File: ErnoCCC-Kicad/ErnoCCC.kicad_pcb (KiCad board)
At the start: 2 copper layers, 161.4 x 95.9 mm, 96 parts, among them J1 6VAC, J2 ICSP, J3 FTDI, J4 Erno Controller, J5 SWITCH, J6 LED OUT, J7 Conn_01x05, Q1 BC847, Q2 BC847, SW1 SW_Push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

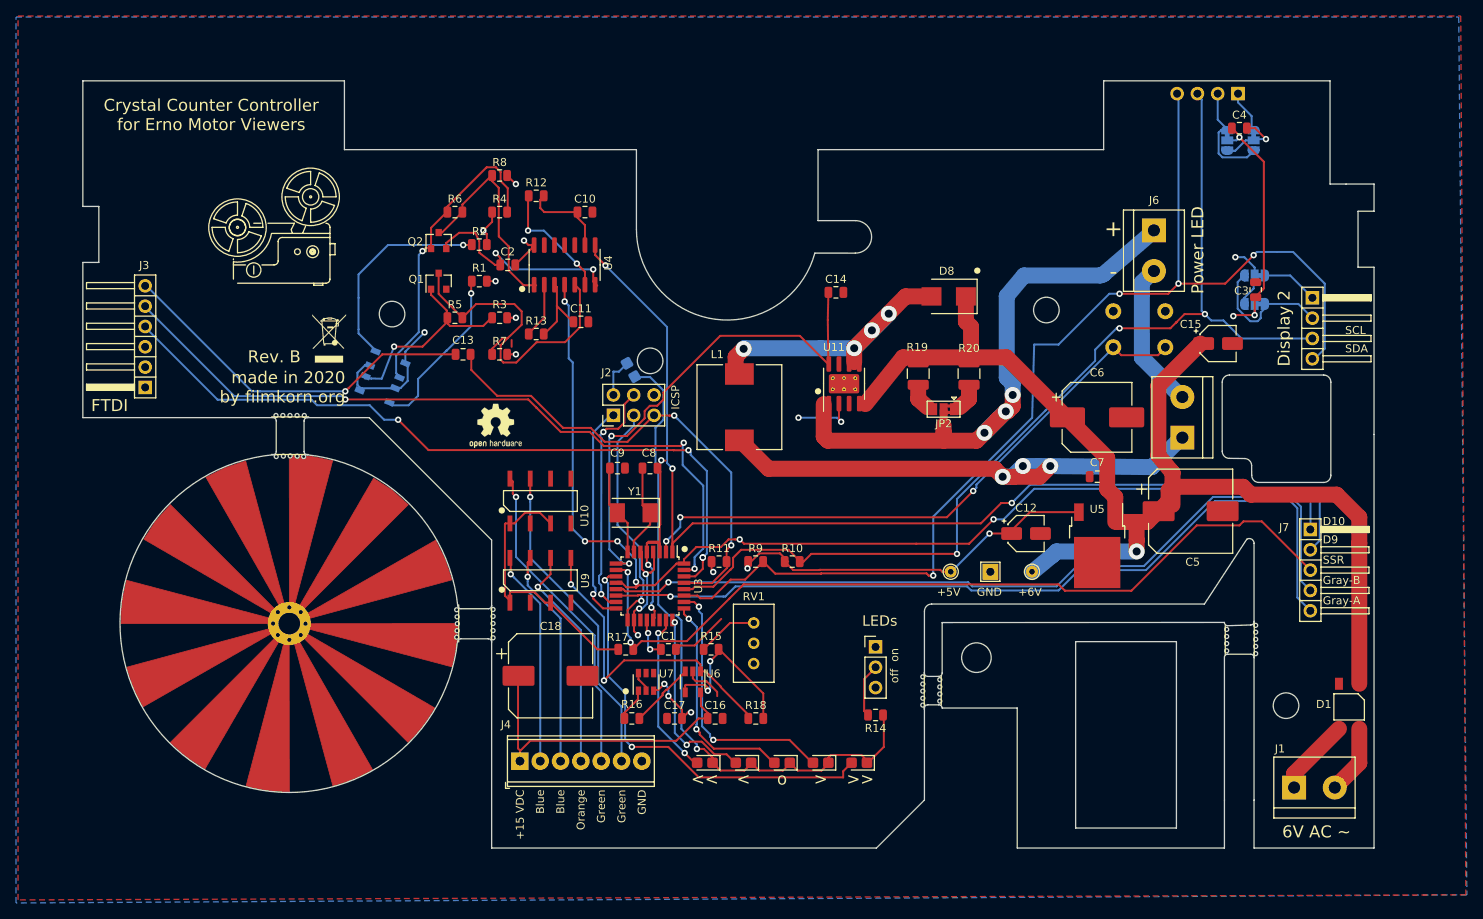
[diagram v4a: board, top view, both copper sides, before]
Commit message: Rounding Corners, making fidicules actually match
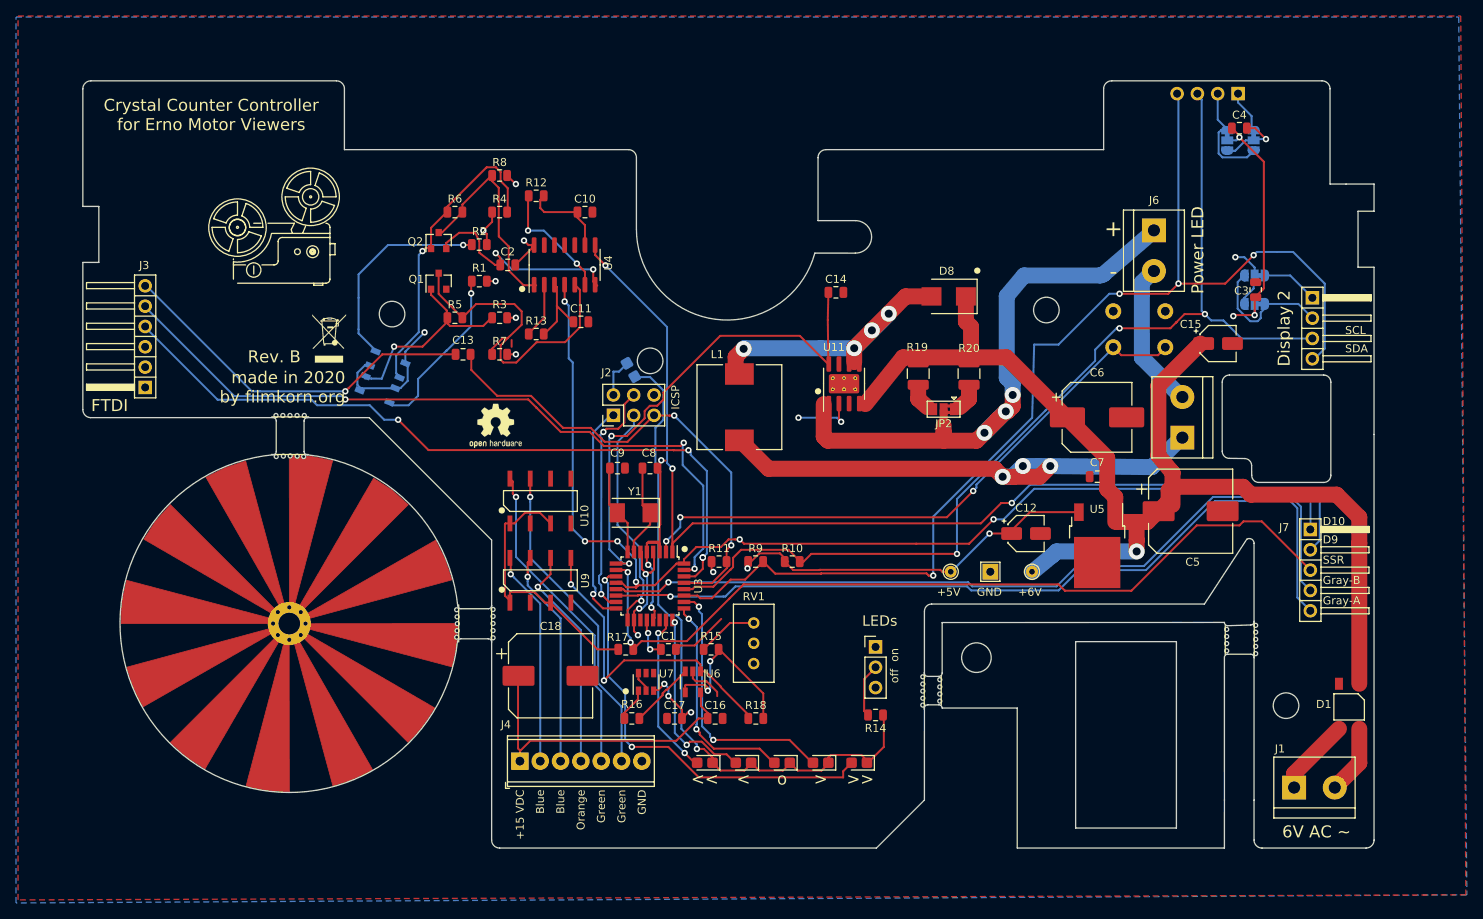
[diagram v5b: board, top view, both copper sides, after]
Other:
- outline, holes or cut-outs redrawn
- board text added: "Cut/Shorten both Jumpers to swap Display polarity"
- board text removed: "Cut/Shorten both Jumpers to swap Display ploarity"
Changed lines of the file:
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@@
   (general
     (thickness 1.6)
-    (drawings 313)
+    (drawings 324)
     (tracks 992)
     (zones 0)
@@
     )
   )
+  (gr_arc (start 218.1 26.2) (end 219.1 26.2) (angle -90) (layer Edge.Cuts) (width 0.05))
+  (gr_arc (start 191.8 26.2) (end 191.8 25.2) (angle -90) (layer Edge.Cuts) (width 0.05))
+  (gr_arc (start 94.9 26.2) (end 95.9 26.2) (angle -90) (layer Edge.Cuts) (width 0.05))
+  (gr_arc (start 64.2 26.2) (end 64.2 25.2) (angle -90) (layer Edge.Cuts) (width 0.05))
+  (gr_arc (start 64.2 66.3) (end 63.2 66.3) (angle -90) (layer Edge.Cuts) (width 0.05))
+  (gr_arc (start 115.3 120.1) (end 114.3 120.1) (angle -90) (layer Edge.Cuts) (width 0.05))
+  (gr_arc (start 223.6 120.1) (end 223.6 121.1) (angle -90) (layer Edge.Cuts) (width 0.05))
+  (gr_arc (start 210.6 120.1) (end 209.6 120.1) (angle -90) (layer Edge.Cuts) (width 0.05))
+  (gr_arc (start 156.1 34.8) (end 156.1 33.8) (angle -90) (layer Edge.Cuts) (width 0.05))
+  (gr_arc (start 131.4 34.8) (end 132.4 34.8) (angle -90) (layer Edge.Cuts) (width 0.05))
+  (gr_circle (center 231.7 71.1) (end 234.7 71.1) (layer F.Paste) (width 0.01))
   (gr_circle (center 52.2 121.1) (end 55.2 121.1) (layer F.Paste) (width 0.01))
   (gr_circle (center 52.2 25.2) (end 55.2 25.2) (layer F.Paste) (width 0.01))
@@
     (effects (font (size 1 1) (thickness 0.15)) (justify right))
   )
-  (gr_text "Cut/Shorten \nboth Jumpers \nto swap Display \nploarity" (at 204 33.1) (layer B.SilkS)
+  (gr_text "Cut/Shorten \nboth Jumpers \nto swap Display \npolarity" (at 204 33.1) (layer B.SilkS)
     (effects (font (size 1 1) (thickness 0.15)) (justify left mirror))
   )
@@
   (gr_line (start 168.401874 103.6066) (end 168.4 115.1) (layer Edge.Cuts) (width 0.05))
   (gr_line (start 205.901874 115.114) (end 205.9 121.1) (layer Edge.Cuts) (width 0.05))
-  (gr_line (start 209.6 115.1) (end 209.6 121.1) (layer Edge.Cuts) (width 0.05))
+  (gr_line (start 209.6 115.1) (end 209.6 120.1) (layer Edge.Cuts) (width 0.05))
   (gr_line (start 170.6118 92.9132) (end 170.6118 99.2378) (layer Edge.Cuts) (width 0.05))
   (gr_line (start 180 103.6) (end 170.6118 103.6) (layer Edge.Cuts) (width 0.05))
@@
   (gr_line (start 209.6 97.282) (end 209.6 115.1) (layer Edge.Cuts) (width 0.05))
   (gr_line (start 209.6008 92.8116) (end 209.6 83) (layer Edge.Cuts) (width 0.05))
-  (gr_line (start 224.6 69.4) (end 224.6 121.1) (layer Edge.Cuts) (width 0.05))
-  (gr_line (start 209.6 121.1) (end 224.6 121.1) (layer Edge.Cuts) (width 0.05))
+  (gr_line (start 224.6 69.4) (end 224.6 120.1) (layer Edge.Cuts) (width 0.05))
+  (gr_line (start 210.6 121.1) (end 223.6 121.1) (layer Edge.Cuts) (width 0.05))
   (gr_arc (start 218.313 62.865) (end 219.202 62.865) (angle -90) (layer Edge.Cuts) (width 0.05))
   (gr_arc (start 206.513 62.865) (end 206.513 61.976) (angle -90) (layer Edge.Cuts) (width 0.05))
@@
   (gr_arc (start 143.75 43.75) (end 132.4 43.75) (angle -164.7617781) (layer Edge.Cuts) (width 0.05))
   (gr_line (start 168.4 115.1) (end 162.4 121.1) (layer Edge.Cuts) (width 0.05))
-  (gr_line (start 63.2 40.9) (end 63.2 25.2) (layer Edge.Cuts) (width 0.05))
+  (gr_line (start 63.2 40.9) (end 63.2 26.2) (layer Edge.Cuts) (width 0.05))
   (gr_line (start 65.2 40.9) (end 63.2 40.9) (layer Edge.Cuts) (width 0.05))
   (gr_line (start 65.2 47.9) (end 65.2 40.9) (layer Edge.Cuts) (width 0.05))
   (gr_line (start 63.2 47.9) (end 65.2 47.9) (layer Edge.Cuts) (width 0.05))
-  (gr_line (start 63.2 67.3) (end 63.2 47.9) (layer Edge.Cuts) (width 0.05))
-  (gr_line (start 86.9696 67.3) (end 63.2 67.3) (layer Edge.Cuts) (width 0.05))
+  (gr_line (start 63.2 66.3) (end 63.2 47.9) (layer Edge.Cuts) (width 0.05))
+  (gr_line (start 86.9696 67.3) (end 64.2 67.3) (layer Edge.Cuts) (width 0.05))
   (gr_line (start 114.3 82.6) (end 99 67.3) (layer Edge.Cuts) (width 0.05))
-  (gr_line (start 114.3 121.1) (end 114.3 95.3516) (layer Edge.Cuts) (width 0.05))
-  (gr_line (start 162.4 121.1) (end 114.3 121.1) (layer Edge.Cuts) (width 0.05))
+  (gr_line (start 114.3 120.1) (end 114.3 95.3516) (layer Edge.Cuts) (width 0.05))
+  (gr_line (start 162.4 121.1) (end 115.3 121.1) (layer Edge.Cuts) (width 0.05))
   (gr_line (start 168.4 91.5) (end 168.4 99.2378) (layer Edge.Cuts) (width 0.05))
   (gr_line (start 203.4 90.6) (end 169.3 90.6) (layer Edge.Cuts) (width 0.05))
@@
   (gr_line (start 221.1 38.1) (end 224.6 38.1) (layer Edge.Cuts) (width 0.05))
   (gr_line (start 219.1 38.1) (end 221.1 38.1) (layer Edge.Cuts) (width 0.05))
-  (gr_line (start 219.1 25.2) (end 219.1 38.1) (layer Edge.Cuts) (width 0.05))
-  (gr_line (start 190.8 25.2) (end 219.1 25.2) (layer Edge.Cuts) (width 0.05))
-  (gr_line (start 190.8 33.8) (end 190.8 25.2) (layer Edge.Cuts) (width 0.05))
-  (gr_line (start 155.1 33.8) (end 190.8 33.8) (layer Edge.Cuts) (width 0.05))
-  (gr_line (start 155.1 42.672) (end 155.1 33.8) (layer Edge.Cuts) (width 0.05))
-  (gr_line (start 132.4 33.8) (end 132.4 43.75) (layer Edge.Cuts) (width 0.05))
-  (gr_line (start 95.9 33.8) (end 132.4 33.8) (layer Edge.Cuts) (width 0.05))
-  (gr_line (start 95.9 25.2) (end 95.9 33.8) (layer Edge.Cuts) (width 0.05))
-  (gr_line (start 63.2 25.2) (end 95.9 25.2) (layer Edge.Cuts) (width 0.05))
+  (gr_line (start 219.1 26.2) (end 219.1 38.1) (layer Edge.Cuts) (width 0.05))
+  (gr_line (start 191.8 25.2) (end 218.1 25.2) (layer Edge.Cuts) (width 0.05))
+  (gr_line (start 190.8 33.8) (end 190.8 26.2) (layer Edge.Cuts) (width 0.05))
+  (gr_line (start 156.1 33.8) (end 190.8 33.8) (layer Edge.Cuts) (width 0.05))
+  (gr_line (start 155.1 42.672) (end 155.1 34.8) (layer Edge.Cuts) (width 0.05))
+  (gr_line (start 132.4 34.8) (end 132.4 43.75) (layer Edge.Cuts) (width 0.05))
+  (gr_line (start 95.9 33.8) (end 131.4 33.8) (layer Edge.Cuts) (width 0.05))
+  (gr_line (start 95.9 26.2) (end 95.9 33.8) (layer Edge.Cuts) (width 0.05))
+  (gr_line (start 64.2 25.2) (end 94.9 25.2) (layer Edge.Cuts) (width 0.05))
   (gr_arc (start 90.025 43.765) (end 89.263 43.765) (angle -30.96375653) (layer F.SilkS) (width 0.12))
   (gr_line (start 91.041 43.384) (end 90.66 44.273) (layer F.SilkS) (width 0.12))

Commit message: Preparing RevC. One Diode still missing
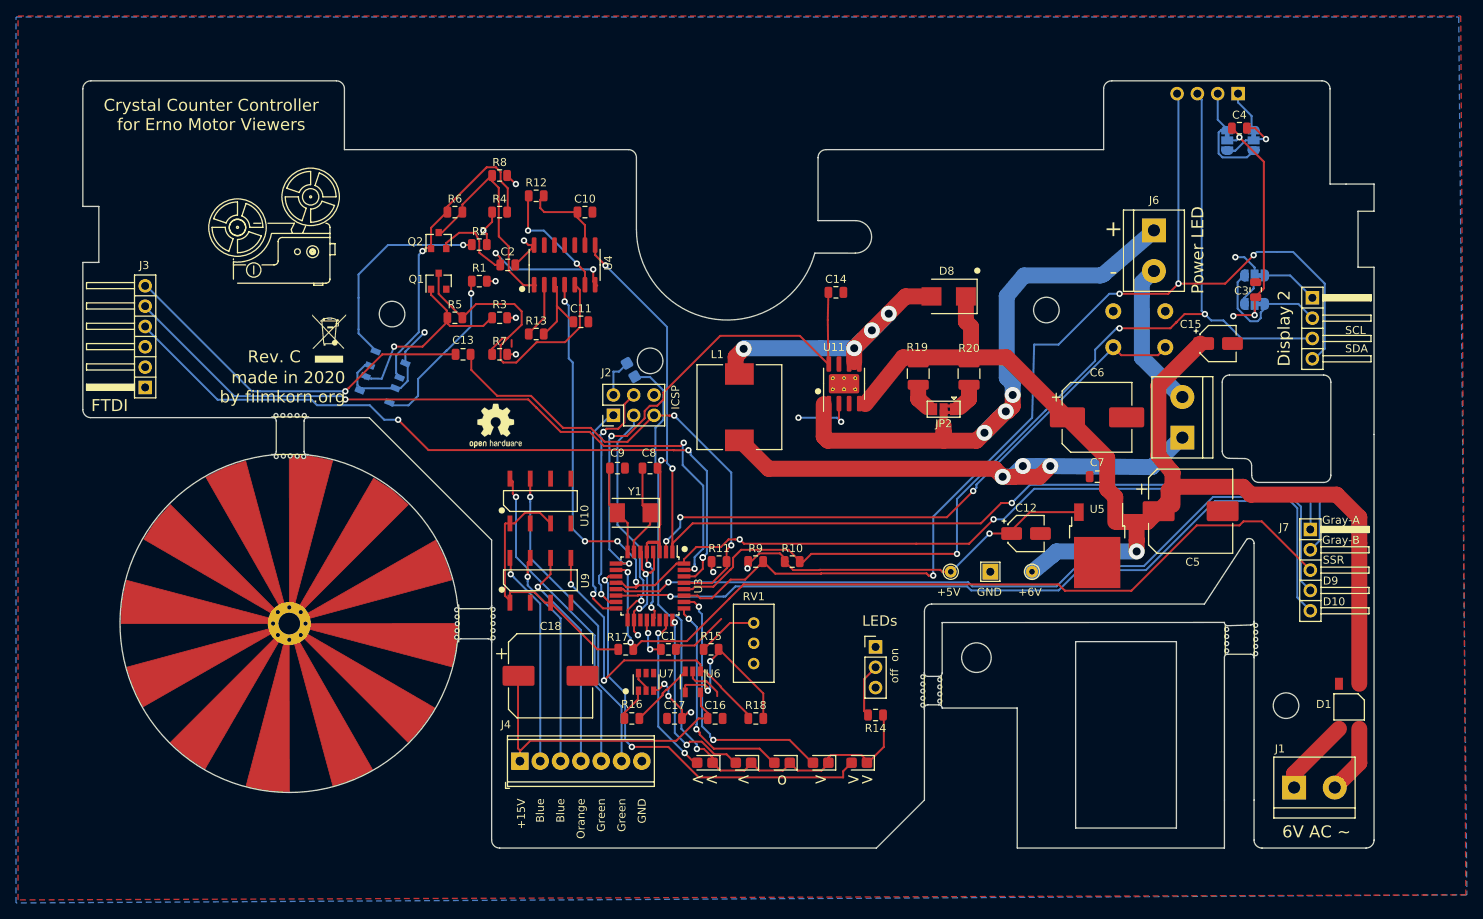
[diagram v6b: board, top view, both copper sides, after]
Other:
- board text added: "+15V"
- board text added: "Rev. C"
- board text removed: "+15 VDC"
- board text removed: "Rev. B"
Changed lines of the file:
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@@
     (effects (font (size 1 1) (thickness 0.15)) (justify left))
   )
-  (gr_text D10 (at 218.186 80.264) (layer F.SilkS)
-    (effects (font (size 1 1) (thickness 0.15)) (justify left))
-  )
-  (gr_text D9 (at 218.186 82.55) (layer F.SilkS)
+  (gr_text D10 (at 218.2 90.3) (layer F.SilkS)
+    (effects (font (size 1 1) (thickness 0.15)) (justify left))
+  )
+  (gr_text D9 (at 218.2 87.7) (layer F.SilkS)
     (effects (font (size 1 1) (thickness 0.15)) (justify left))
   )
@@
     (effects (font (size 1 1) (thickness 0.15)) (justify left))
   )
-  (gr_text Gray-B (at 218.186 87.63) (layer F.SilkS)
-    (effects (font (size 1 1) (thickness 0.15)) (justify left))
-  )
-  (gr_text Gray-A (at 218.186 90.17) (layer F.SilkS)
-    (effects (font (size 1 1) (thickness 0.15)) (justify left))
-  )
-  (gr_text GND (at 133.096 113.792 90) (layer F.SilkS)
-    (effects (font (size 1 1) (thickness 0.15)) (justify right))
-  )
-  (gr_text "+15 VDC" (at 117.856 113.792 90) (layer F.SilkS)
+  (gr_text Gray-B (at 218.1 82.6) (layer F.SilkS)
+    (effects (font (size 1 1) (thickness 0.15)) (justify left))
+  )
+  (gr_text Gray-A (at 218.1 80.1) (layer F.SilkS)
+    (effects (font (size 1 1) (thickness 0.15)) (justify left))
+  )
+  (gr_text GND (at 133.096 114.892 90) (layer F.SilkS)
+    (effects (font (size 1 1) (thickness 0.15)) (justify right))
+  )
+  (gr_text +15V (at 118 114.9 90) (layer F.SilkS)
     (effects (font (size 1 1) (thickness 0.15)) (justify right))
   )
@@
   (gr_circle (center 82.532 43.547102) (end 85.072 46.087102) (layer F.SilkS) (width 0.12))
   (gr_circle (center 91.676 39.701) (end 94.216 42.241) (layer F.SilkS) (width 0.12))
-  (gr_text "Rev. B" (at 87.122 59.69) (layer F.SilkS)
+  (gr_text "Rev. C" (at 87.122 59.69) (layer F.SilkS)
     (effects (font (size 1.5 1.5) (thickness 0.3)))
   )
@@
     (effects (font (size 1.5 1.5) (thickness 0.3)))
   )
-  (gr_text Green (at 130.556 113.792 90) (layer F.SilkS)
-    (effects (font (size 1 1) (thickness 0.15)) (justify right))
-  )
-  (gr_text Green (at 127.998 113.792 90) (layer F.SilkS)
-    (effects (font (size 1 1) (thickness 0.15)) (justify right))
-  )
-  (gr_text Blue (at 120.378 113.792 90) (layer F.SilkS)
-    (effects (font (size 1 1) (thickness 0.15)) (justify right))
-  )
-  (gr_text Blue (at 122.918 113.792 90) (layer F.SilkS)
-    (effects (font (size 1 1) (thickness 0.15)) (justify right))
-  )
-  (gr_text Orange (at 125.458 113.792 90) (layer F.SilkS)
-    (effects (font (size 1 1) (thickness 0.15)) (justify right))
-  )
+  (gr_text Green (at 130.556 114.892 90) (layer F.SilkS)
+    (effects (font (size 1 1) (thickness 0.15)) (justify right))
+  )
+  (gr_text Green (at 127.998 114.892 90) (layer F.SilkS)
+    (effects (font (size 1 1) (thickness 0.15)) (justify right))
+  )
+  (gr_text Blue (at 120.378 114.892 90) (layer F.SilkS)
+    (effects (font (size 1 1) (thickness 0.15)) (justify right))
+  )
+  (gr_text Blue (at 122.918 114.892 90) (layer F.SilkS)
+    (effects (font (size 1 1) (thickness 0.15)) (justify right))
+  )
+  (gr_text Orange (at 125.458 114.892 90) (layer F.SilkS)
+    (effects (font (size 1 1) (thickness 0.15)) (justify right))
+  )
